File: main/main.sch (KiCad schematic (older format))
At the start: 34 parts, among them J1 Conn_01x10_Female, J2 USB_B, J3 AVR-ISP-6, J4 Micro_SD_Card, Q1 2N7002, Q2 BSS84, SW1 Reset, U1 ATmega1284P-PU, U2 AMS1117, U3 MCP2221A-I_SL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

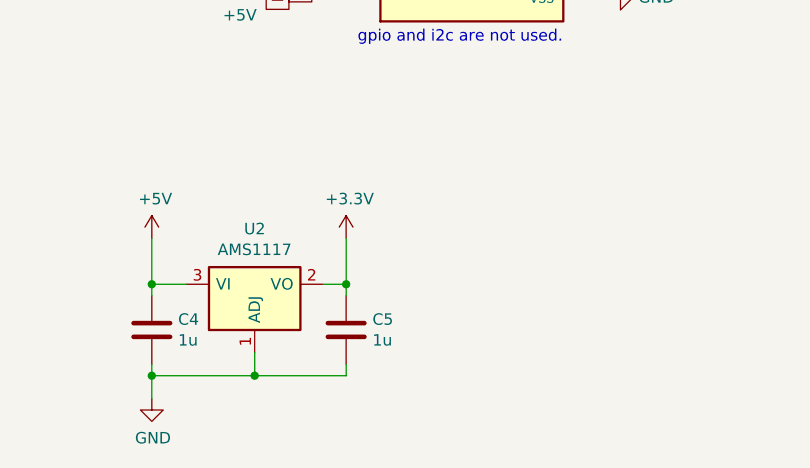
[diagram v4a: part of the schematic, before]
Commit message: fixed 3.3v regulator cap
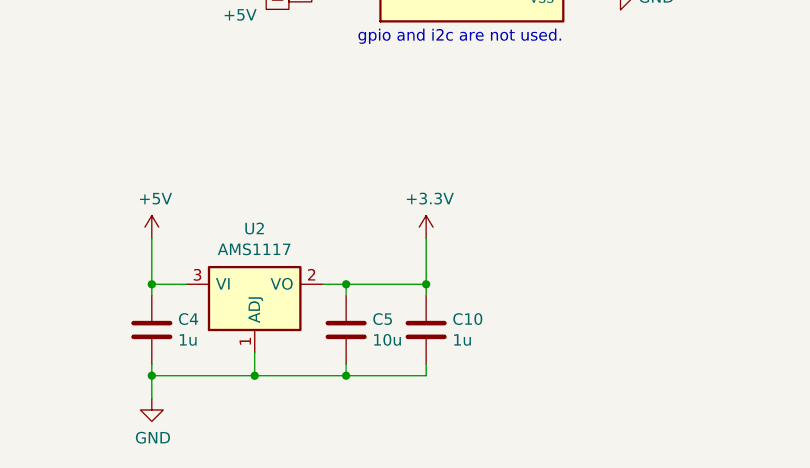
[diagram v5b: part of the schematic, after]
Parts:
- added C10: 1u, Capacitor_SMD:C_1206_3216Metric, symbol Device:C
- C5: value 1u -> 10u
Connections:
- net +3V3: now also C10.1
- net GND: now also C10.2
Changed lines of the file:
@@
 P 5450 7100
 F 0 "C5" H 5565 7146 50  0000 L CNN
-F 1 "1u" H 5565 7055 50  0000 L CNN
+F 1 "10u" H 5565 7055 50  0000 L CNN
 F 2 "Capacitor_SMD:C_1206_3216Metric" H 5488 6950 50  0001 C CNN
 F 3 "~" H 5450 7100 50  0001 C CNN
@@
 L power:+3.3V #PWR020
 U 1 1 69377217
-P 5450 6700
-F 0 "#PWR020" H 5450 6550 50  0001 C CNN
-F 1 "+3.3V" H 5465 6873 50  0000 C CNN
-F 2 "" H 5450 6700 50  0001 C CNN
-F 3 "" H 5450 6700 50  0001 C CNN
-	1    5450 6700
-	1    0    0    -1
-$EndComp
-Wire Wire Line
-	5450 6700 5450 6900
+P 5800 6700
+F 0 "#PWR020" H 5800 6550 50  0001 C CNN
+F 1 "+3.3V" H 5815 6873 50  0000 C CNN
+F 2 "" H 5800 6700 50  0001 C CNN
+F 3 "" H 5800 6700 50  0001 C CNN
+	1    5800 6700
+	1    0    0    -1
+$EndComp
 Wire Wire Line
 	5450 6900 5350 6900
-Connection ~ 5450 6900
 Wire Wire Line
 	5450 6900 5450 6950
@@
 	1    0    0    -1
 $EndComp
+$Comp
+L Device:C C10
+U 1 1 693AEFEF
+P 5800 7100
+F 0 "C10" H 5915 7146 50  0000 L CNN
+F 1 "1u" H 5915 7055 50  0000 L CNN
+F 2 "Capacitor_SMD:C_1206_3216Metric" H 5838 6950 50  0001 C CNN
+F 3 "~" H 5800 7100 50  0001 C CNN
+	1    5800 7100
+	1    0    0    -1
+$EndComp
+Wire Wire Line
+	5450 6900 5800 6900
+Connection ~ 5450 6900
+Wire Wire Line
+	5800 6700 5800 6900
+Connection ~ 5800 6900
+Wire Wire Line
+	5800 6900 5800 6950
+Wire Wire Line
+	5450 7300 5800 7300
+Wire Wire Line
+	5800 7300 5800 7250
+Connection ~ 5450 7300
 $EndSCHEMATC

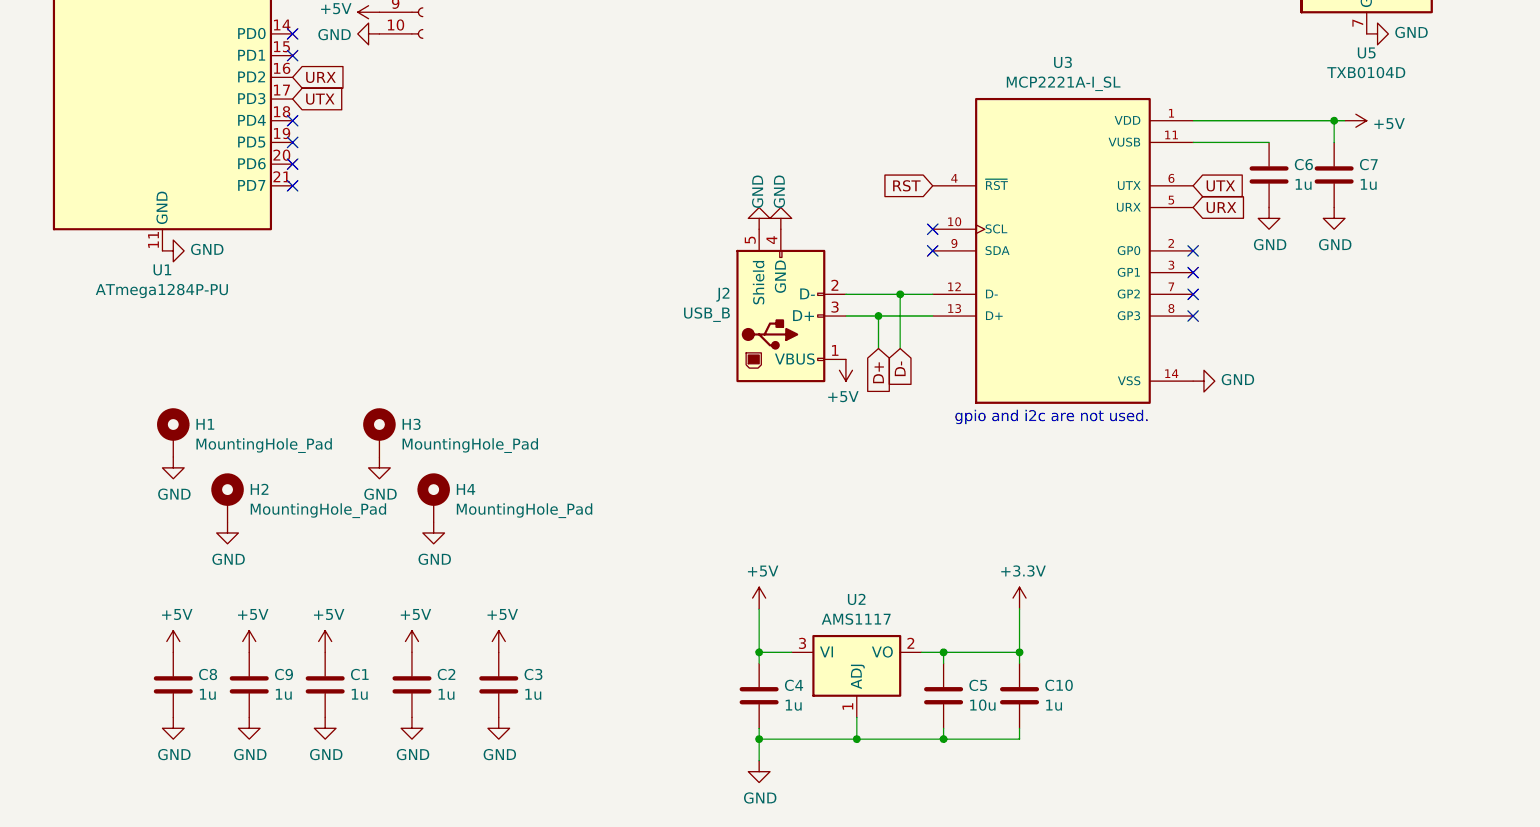
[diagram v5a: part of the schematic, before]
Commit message: fixed bulking caps
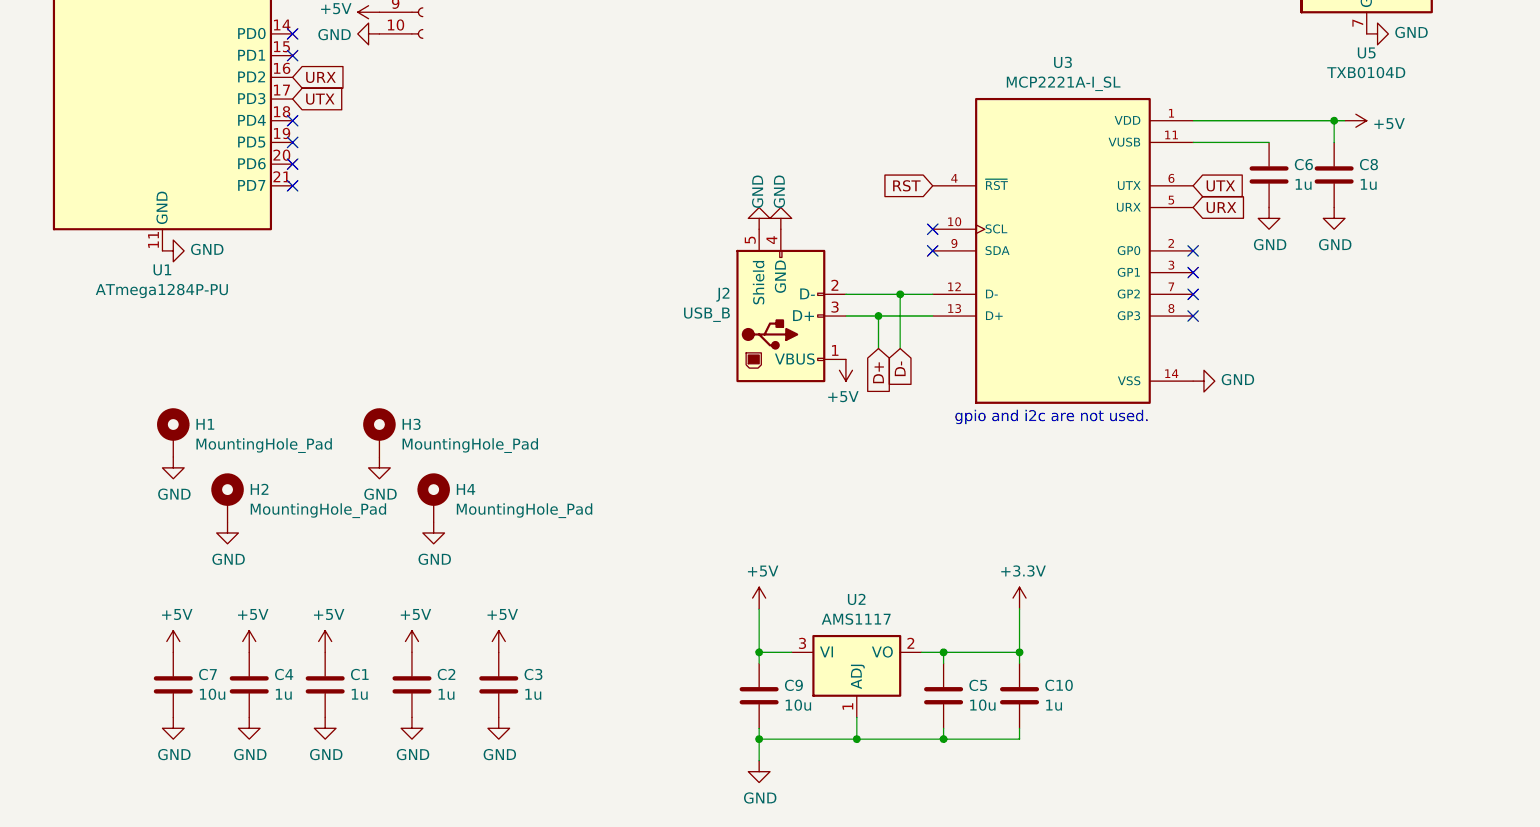
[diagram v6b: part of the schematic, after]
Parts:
- C7, C9: value 1u -> 10u
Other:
- moved on the sheet: C4, C7, C8, C9
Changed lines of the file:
@@
 L Device:C C4
 U 1 1 6937311A
-P 4600 7100
-F 0 "C4" H 4715 7146 50  0000 L CNN
-F 1 "1u" H 4715 7055 50  0000 L CNN
-F 2 "Capacitor_SMD:C_1206_3216Metric" H 4638 6950 50  0001 C CNN
-F 3 "~" H 4600 7100 50  0001 C CNN
-	1    4600 7100
+P 2250 7050
+F 0 "C4" H 2365 7096 50  0000 L CNN
+F 1 "1u" H 2365 7005 50  0000 L CNN
+F 2 "Capacitor_SMD:C_1206_3216Metric" H 2288 6900 50  0001 C CNN
+F 3 "~" H 2250 7050 50  0001 C CNN
+	1    2250 7050
 	1    0    0    -1
 $EndComp
@@
 L Device:C C7
 U 1 1 692C9AB5
-P 7250 4700
-F 0 "C7" H 7135 4654 50  0000 R CNN
-F 1 "1u" H 7135 4745 50  0000 R CNN
-F 2 "Capacitor_SMD:C_1206_3216Metric" H 7288 4550 50  0001 C CNN
-F 3 "~" H 7250 4700 50  0001 C CNN
-	1    7250 4700
+P 1900 7050
+F 0 "C7" H 1785 7004 50  0000 R CNN
+F 1 "10u" H 1785 7095 50  0000 R CNN
+F 2 "Capacitor_SMD:C_1206_3216Metric" H 1938 6900 50  0001 C CNN
+F 3 "~" H 1900 7050 50  0001 C CNN
+	1    1900 7050
 	-1   0    0    1
 $EndComp
@@
 L power:GND #PWR027
 U 1 1 692C9ABB
-P 7250 4850
-F 0 "#PWR027" H 7250 4600 50  0001 C CNN
-F 1 "GND" H 7255 4677 50  0000 C CNN
-F 2 "" H 7250 4850 50  0001 C CNN
-F 3 "" H 7250 4850 50  0001 C CNN
-	1    7250 4850
+P 1900 7200
+F 0 "#PWR027" H 1900 6950 50  0001 C CNN
+F 1 "GND" H 1905 7027 50  0000 C CNN
+F 2 "" H 1900 7200 50  0001 C CNN
+F 3 "" H 1900 7200 50  0001 C CNN
+	1    1900 7200
 	1    0    0    -1
 $EndComp
@@
 L Device:C C9
 U 1 1 692B4C36
-P 2250 7050
-F 0 "C9" H 2365 7096 50  0000 L CNN
-F 1 "1u" H 2365 7005 50  0000 L CNN
-F 2 "Capacitor_SMD:C_1206_3216Metric" H 2288 6900 50  0001 C CNN
-F 3 "~" H 2250 7050 50  0001 C CNN
-	1    2250 7050
+P 4600 7100
+F 0 "C9" H 4715 7146 50  0000 L CNN
+F 1 "10u" H 4715 7055 50  0000 L CNN
+F 2 "Capacitor_SMD:C_1206_3216Metric" H 4638 6950 50  0001 C CNN
+F 3 "~" H 4600 7100 50  0001 C CNN
+	1    4600 7100
 	1    0    0    -1
 $EndComp
@@
 L power:GND #PWR044
 U 1 1 692B6620
-P 1900 7200
-F 0 "#PWR044" H 1900 6950 50  0001 C CNN
-F 1 "GND" H 1905 7027 50  0000 C CNN
-F 2 "" H 1900 7200 50  0001 C CNN
-F 3 "" H 1900 7200 50  0001 C CNN
-	1    1900 7200
+P 7250 4850
+F 0 "#PWR044" H 7250 4600 50  0001 C CNN
+F 1 "GND" H 7255 4677 50  0000 C CNN
+F 2 "" H 7250 4850 50  0001 C CNN
+F 3 "" H 7250 4850 50  0001 C CNN
+	1    7250 4850
 	1    0    0    -1
 $EndComp
@@
 L Device:C C8
 U 1 1 692B6626
-P 1900 7050
-F 0 "C8" H 2015 7096 50  0000 L CNN
-F 1 "1u" H 2015 7005 50  0000 L CNN
-F 2 "Capacitor_SMD:C_1206_3216Metric" H 1938 6900 50  0001 C CNN
-F 3 "~" H 1900 7050 50  0001 C CNN
-	1    1900 7050
-	1    0    0    -1
-$EndComp
+P 7250 4700
+F 0 "C8" H 7365 4746 50  0000 L CNN
+F 1 "1u" H 7365 4655 50  0000 L CNN
+F 2 "Capacitor_SMD:C_1206_3216Metric" H 7288 4550 50  0001 C CNN
+F 3 "~" H 7250 4700 50  0001 C CNN
+	1    7250 4700
+	1    0    0    -1
+$EndComp
